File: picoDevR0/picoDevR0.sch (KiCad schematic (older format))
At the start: 17 parts, among them J1 Barrel_Jack, J2 Pico1to20, SW1 SW_Push_Dual

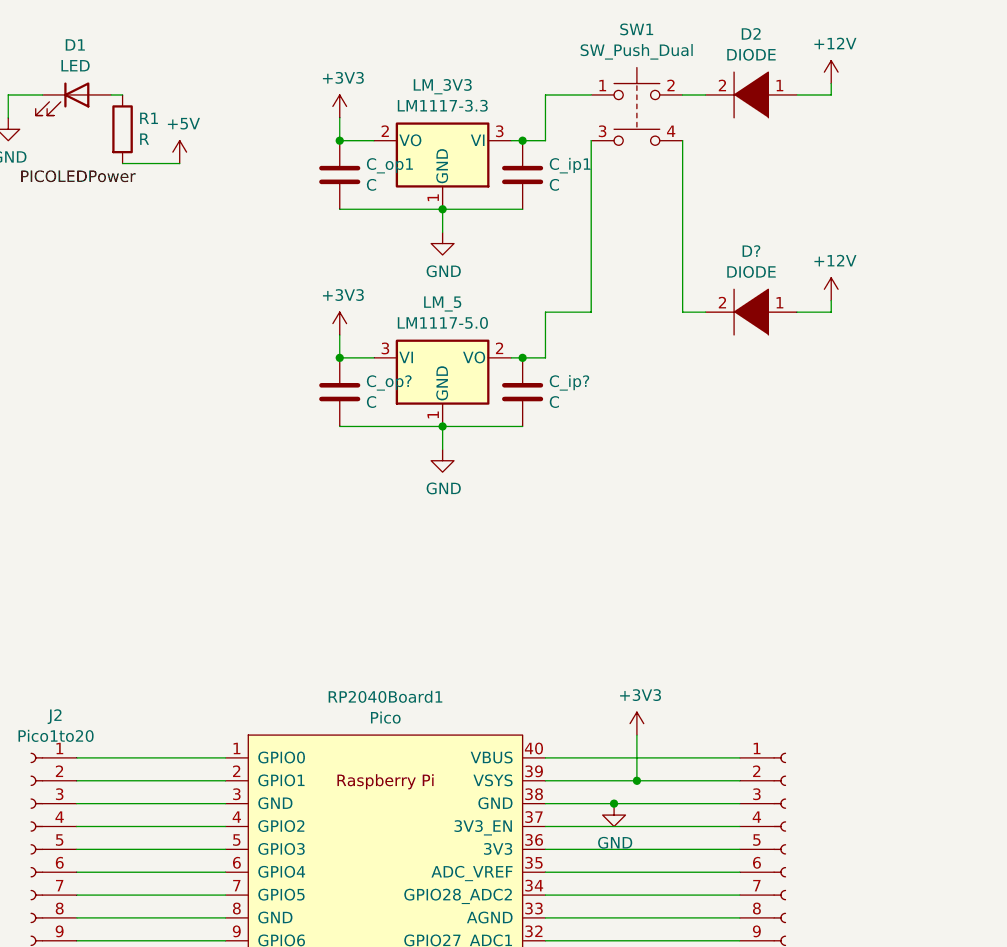
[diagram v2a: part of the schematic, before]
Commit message: added 5V layer
added everything to the PCB. 
issues: 5V layer is not getting connected with the pico Vcc and the LED resistor for some reason, needs debugging.
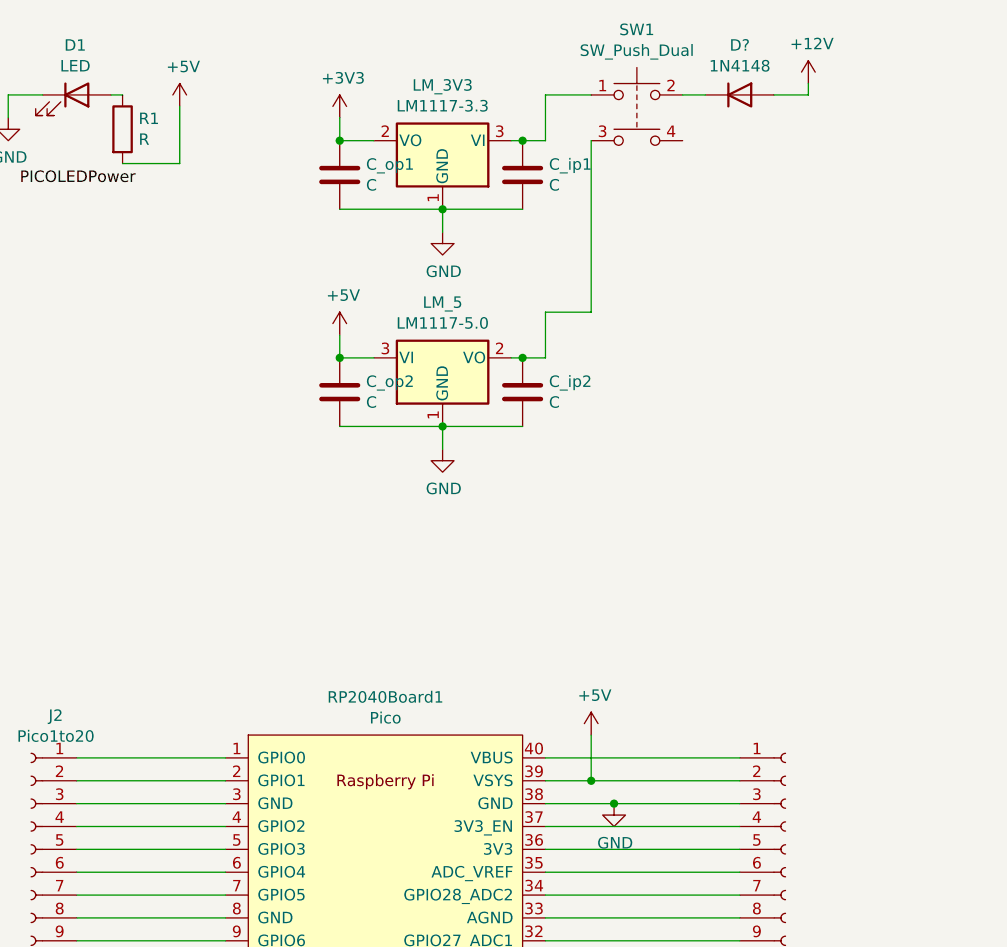
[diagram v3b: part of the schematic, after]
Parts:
- removed D2, D?: DIODE, Diode_THT:D_5W_P10.16mm_Horizontal, symbol pspice:DIODE
- added D?: 1N4148, Diode_THT:D_DO-35_SOD27_P7.62mm_Horizontal, symbol Diode:1N4148
- LM_5: footprint (none) -> Connector_PinSocket_1.00mm:PinSocket_1x03_P1.00mm_Vertical
- SW1: footprint Button_Switch_THT:SW_PUSH-12mm -> Button_Switch_THT:Push_E-Switch_KS01Q01
- gave numbers to parts that had none: 2
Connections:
- net +12V: now also D?.2 (A)
- net +3V3: no longer C_op2.1, LM_5.3 (VI), RP2040Board1.39 (VSYS), pico21to40.2 (Pin_2)
- net +5V: now also C_op2.1, LM_5.3 (VI), RP2040Board1.39 (VSYS), pico21to40.2 (Pin_2)
- net at SW1.2: now also D?.1 (K)
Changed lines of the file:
@@
 F 0 "SW1" H 5800 1135 50  0000 C CNN
 F 1 "SW_Push_Dual" H 5800 1044 50  0000 C CNN
-F 2 "Button_Switch_THT:SW_PUSH-12mm" H 5800 1050 50  0001 C CNN
+F 2 "Button_Switch_THT:Push_E-Switch_KS01Q01" H 5800 1050 50  0001 C CNN
 F 3 "~" H 5800 1050 50  0001 C CNN
 	1    5800 850
@@
 	5300 1050 5400 1050
 Connection ~ 4950 1350
-$Comp
-L power:+5V #PWR0106
-U 1 1 60A98CEA
-P 3800 1150
-F 0 "#PWR0106" H 3800 1000 50  0001 C CNN
-F 1 "+5V" H 3815 1323 50  0000 C CNN
-F 2 "" H 3800 1150 50  0001 C CNN
-F 3 "" H 3800 1150 50  0001 C CNN
-	1    3800 1150
-	1    0    0    -1
-$EndComp
 Wire Wire Line
 	3550 1150 3800 1150
@@
 Text Label 3100 1250 0    50   ~ 0
 PICOLEDPower
-$Comp
-L pspice:DIODE D2
-U 1 1 60AC61B3
-P 6300 850
-F 0 "D2" H 6300 585 50  0000 C CNN
-F 1 "DIODE" H 6300 676 50  0000 C CNN
-F 2 "Diode_THT:D_5W_P10.16mm_Horizontal" H 6300 850 50  0001 C CNN
-F 3 "~" H 6300 850 50  0001 C CNN
-	1    6300 850
-	-1   0    0    1
-$EndComp
 $Comp
 L power:+12V #PWR0107
@@
 L power:+12V #PWR0109
 U 1 1 60B08677
-P 6650 800
-F 0 "#PWR0109" H 6650 650 50  0001 C CNN
-F 1 "+12V" H 6665 973 50  0000 C CNN
-F 2 "" H 6650 800 50  0001 C CNN
-F 3 "" H 6650 800 50  0001 C CNN
-	1    6650 800
-	1    0    0    -1
-$EndComp
-Wire Wire Line
-	6650 800  6650 850
-Wire Wire Line
-	6650 850  6500 850
+P 6550 800
+F 0 "#PWR0109" H 6550 650 50  0001 C CNN
+F 1 "+12V" H 6565 973 50  0000 C CNN
+F 2 "" H 6550 800 50  0001 C CNN
+F 3 "" H 6550 800 50  0001 C CNN
+	1    6550 800
+	1    0    0    -1
+$EndComp
+Wire Wire Line
+	6550 800  6550 850
+Wire Wire Line
+	6550 850  6400 850
 $Comp
 L power:GND #PWR0110
@@
 	1    0    0    -1
 $EndComp
-$Comp
-L power:+3V3 #PWR0104
-U 1 1 60C0C28A
-P 5800 3650
-F 0 "#PWR0104" H 5800 3500 50  0001 C CNN
-F 1 "+3V3" H 5815 3823 50  0000 C CNN
-F 2 "" H 5800 3650 50  0001 C CNN
-F 3 "" H 5800 3650 50  0001 C CNN
-	1    5800 3650
-	1    0    0    -1
-$EndComp
-Wire Wire Line
-	5400 3850 5800 3850
-Wire Wire Line
-	5800 3650 5800 3850
-Connection ~ 5800 3850
-Wire Wire Line
-	5800 3850 6250 3850
 Wire Wire Line
 	4950 2300 5300 2300
@@
 	4500 2000 4500 1900
 $Comp
-L Device:C C_op?
+L Device:C C_op2
 U 1 1 60C2267B
 P 4500 2150
-F 0 "C_op?" H 4615 2196 50  0000 L CNN
+F 0 "C_op2" H 4615 2196 50  0000 L CNN
 F 1 "C" H 4615 2105 50  0000 L CNN
 F 2 "Capacitor_THT:CP_Radial_D10.0mm_P2.50mm" H 4538 2000 50  0001 C CNN
@@
 $EndComp
 $Comp
-L Device:C C_ip?
+L Device:C C_ip2
 U 1 1 60C22681
 P 5300 2150
-F 0 "C_ip?" H 5415 2196 50  0000 L CNN
+F 0 "C_ip2" H 5415 2196 50  0000 L CNN
 F 1 "C" H 5415 2105 50  0000 L CNN
 F 2 "Capacitor_THT:CP_Radial_D10.0mm_P2.50mm" H 5338 2000 50  0001 C CNN
@@
 	5300 2000 5400 2000
 Connection ~ 4950 2300
-$Comp
-L pspice:DIODE D?
-U 1 1 60C2268A
-P 6300 1800
-F 0 "D?" H 6300 1535 50  0000 C CNN
-F 1 "DIODE" H 6300 1626 50  0000 C CNN
-F 2 "Diode_THT:D_5W_P10.16mm_Horizontal" H 6300 1800 50  0001 C CNN
-F 3 "~" H 6300 1800 50  0001 C CNN
-	1    6300 1800
-	-1   0    0    1
-$EndComp
-$Comp
-L power:+12V #PWR?
-U 1 1 60C22690
-P 6650 1750
-F 0 "#PWR?" H 6650 1600 50  0001 C CNN
-F 1 "+12V" H 6665 1923 50  0000 C CNN
-F 2 "" H 6650 1750 50  0001 C CNN
-F 3 "" H 6650 1750 50  0001 C CNN
-	1    6650 1750
-	1    0    0    -1
-$EndComp
-Wire Wire Line
-	6650 1750 6650 1800
-Wire Wire Line
-	6650 1800 6500 1800
-Wire Wire Line
-	6100 1800 6000 1800
 Connection ~ 4500 2000
 Wire Wire Line
 	4500 2300 4950 2300
 $Comp
-L power:GND #PWR?
+L power:GND #PWR0113
 U 1 1 60C2269B
 P 4950 2400
-F 0 "#PWR?" H 4950 2150 50  0001 C CNN
+F 0 "#PWR0113" H 4950 2150 50  0001 C CNN
 F 1 "GND" H 4955 2227 50  0000 C CNN
 F 2 "" H 4950 2400 50  0001 C CNN
@@
 Wire Wire Line
 	4950 2400 4950 2300
-$Comp
-L power:+3V3 #PWR?
-U 1 1 60C226A2
-P 4500 1900
-F 0 "#PWR?" H 4500 1750 50  0001 C CNN
-F 1 "+3V3" H 4515 2073 50  0000 C CNN
-F 2 "" H 4500 1900 50  0001 C CNN
-F 3 "" H 4500 1900 50  0001 C CNN
-	1    4500 1900
-	1    0    0    -1
-$EndComp
 $Comp
 L Regulator_Linear:LM1117-5.0 LM_5
@@
 F 0 "LM_5" H 4950 2242 50  0000 C CNN
 F 1 "LM1117-5.0" H 4950 2151 50  0000 C CNN
-F 2 "" H 4950 2000 50  0001 C CNN
+F 2 "Connector_PinSocket_1.00mm:PinSocket_1x03_P1.00mm_Vertical" H 4950 2000 50  0001 C CNN
 F 3 "http://www.ti.com/lit/ds/symlink/lm1117.pdf" H 4950 2000 50  0001 C CNN
 	1    4950 2000
@@
 Wire Wire Line
 	5600 1050 5600 1800
-Wire Wire Line
-	6000 1050 6000 1800
+$Comp
+L power:+5V #PWR0112
+U 1 1 60C58578
+P 4500 1900
+F 0 "#PWR0112" H 4500 1750 50  0001 C CNN
+F 1 "+5V" H 4515 2073 50  0000 C CNN
+F 2 "" H 4500 1900 50  0001 C CNN
+F 3 "" H 4500 1900 50  0001 C CNN
+	1    4500 1900
+	1    0    0    -1
+$EndComp
+Wire Wire Line
+	5600 3650 5600 3850
+Wire Wire Line
+	5600 3850 6250 3850
+$Comp
+L power:+5V #PWR0104
+U 1 1 60C7459A
+P 3800 900
+F 0 "#PWR0104" H 3800 750 50  0001 C CNN
+F 1 "+5V" H 3815 1073 50  0000 C CNN
+F 2 "" H 3800 900 50  0001 C CNN
+F 3 "" H 3800 900 50  0001 C CNN
+	1    3800 900
+	1    0    0    -1
+$EndComp
+$Comp
+L power:+5V #PWR0106
+U 1 1 60C79A6B
+P 5600 3650
+F 0 "#PWR0106" H 5600 3500 50  0001 C CNN
+F 1 "+5V" H 5615 3823 50  0000 C CNN
+F 2 "" H 5600 3650 50  0001 C CNN
+F 3 "" H 5600 3650 50  0001 C CNN
+	1    5600 3650
+	1    0    0    -1
+$EndComp
+Wire Wire Line
+	3800 1150 3800 900
+Wire Wire Line
+	5400 3850 5600 3850
+Connection ~ 5600 3850
+$Comp
+L Diode:1N4148 D?
+U 1 1 60CAB248
+P 6250 850
+F 0 "D?" H 6250 1067 50  0000 C CNN
+F 1 "1N4148" H 6250 976 50  0000 C CNN
+F 2 "Diode_THT:D_DO-35_SOD27_P7.62mm_Horizontal" H 6250 675 50  0001 C CNN
+F 3 "https://assets.nexperia.com/documents/data-sheet/1N4148_1N4448.pdf" H 6250 850 50  0001 C CNN
+	1    6250 850
+	1    0    0    -1
+$EndComp
 $EndSCHEMATC

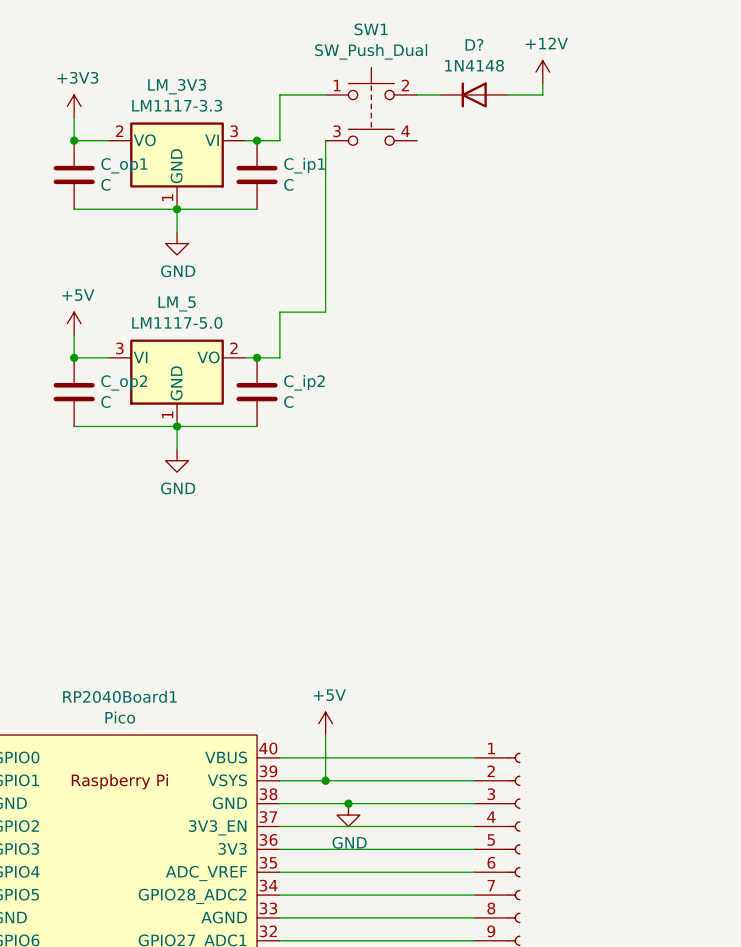
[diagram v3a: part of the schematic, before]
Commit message: updated README
Updated photos
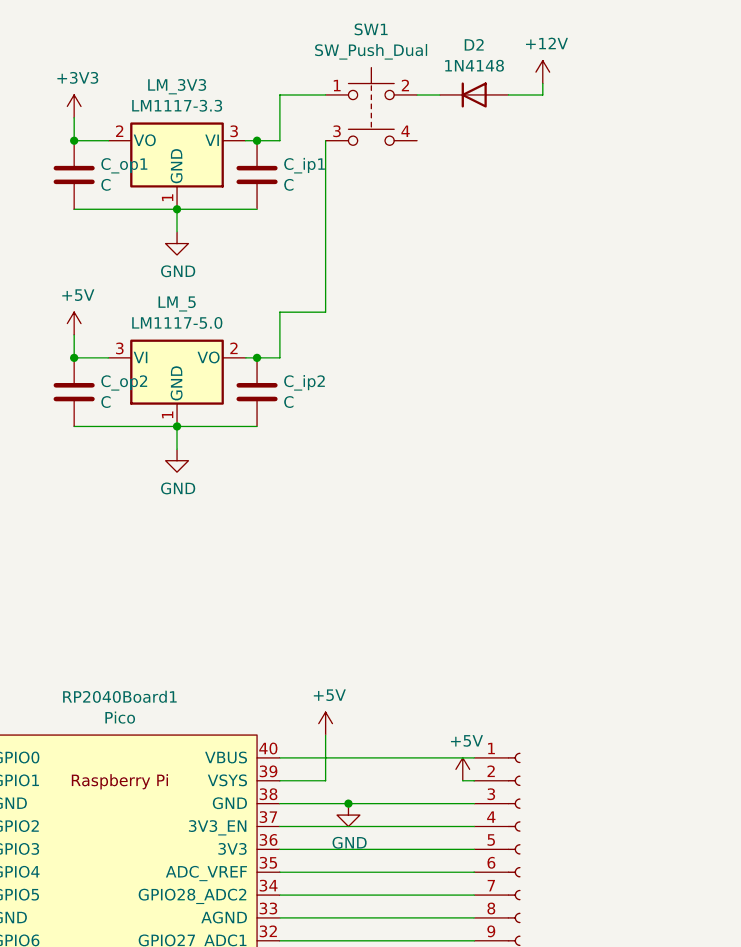
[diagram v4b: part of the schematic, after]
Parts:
- gave numbers to parts that had none: 1
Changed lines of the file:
@@
 Wire Wire Line
 	5600 3650 5600 3850
-Wire Wire Line
-	5600 3850 6250 3850
 $Comp
 L power:+5V #PWR0104
@@
 Wire Wire Line
 	5400 3850 5600 3850
-Connection ~ 5600 3850
 $Comp
-L Diode:1N4148 D?
+L Diode:1N4148 D2
 U 1 1 60CAB248
 P 6250 850
-F 0 "D?" H 6250 1067 50  0000 C CNN
+F 0 "D2" H 6250 1067 50  0000 C CNN
 F 1 "1N4148" H 6250 976 50  0000 C CNN
 F 2 "Diode_THT:D_DO-35_SOD27_P7.62mm_Horizontal" H 6250 675 50  0001 C CNN
@@
 	1    0    0    -1
 $EndComp
+$Comp
+L power:+5V #PWR0114
+U 1 1 60CB5175
+P 6200 3850
+F 0 "#PWR0114" H 6200 3700 50  0001 C CNN
+F 1 "+5V" H 6215 4023 50  0000 C CNN
+F 2 "" H 6200 3850 50  0001 C CNN
+F 3 "" H 6200 3850 50  0001 C CNN
+	1    6200 3850
+	1    0    0    -1
+$EndComp
+Wire Wire Line
+	6250 3850 6200 3850
 $EndSCHEMATC
